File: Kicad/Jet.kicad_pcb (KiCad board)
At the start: 2 copper layers, 17 parts, among them J1 Conn_02x13_Odd_Even, J2 Conn_01x03_Female, J3 POWER, J4 Conn_02x10_Odd_Even, J5 Conn_02x10_Odd_Even, Q1 Q_NPN_EBC, Q2 Q_NPN_EBC, U1 PC817, U2 PC817

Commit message: UPDATE: footprint
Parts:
- D1, D3: value D_Zener -> BZM55C30-LGE; footprint Diode_THT:D_DO-35_SOD27_P7.62mm_Horizontal -> Diode_SMD:D_MiniMELF
- D2, D4: value 1N4448 -> M7L-DIO; footprint Diode_THT:D_DO-35_SOD27_P7.62mm_Horizontal -> Diode_SMD:D_SMA
- Q1, Q2: value Q_NPN_EBC -> BCW66FR; footprint Package_TO_SOT_THT:TO-92L_HandSolder -> Package_TO_SOT_SMD:SOT-23
- moved R3 85.3 mm to (112.6, 149.2), turned to 180 degrees
- moved D4 82.6 mm to (154.0, 29.6), turned to -90 degrees
- moved D3 80.8 mm to (156.9, 29.6)
- moved Q2 69.1 mm to (156.7, 40.8), turned to 180 degrees
- moved R4 68.0 mm to (156.3, 57.3), turned to 0 degrees
- moved R2 62.6 mm to (156.3, 45.0)
- moved U1 61.5 mm to (96.8, 139.5), turned to 180 degrees
- moved U2 57.1 mm to (154.1, 54.9)
- moved D1 55.0 mm to (112.6, 25.6), turned to 90 degrees
- moved D2 50.0 mm to (109.1, 25.8), turned to 90 degrees
- moved J1 23.2 mm to (96.6, 105.1)
- moved Q1 15.5 mm to (90.8, 60.9)
- moved R1 15.5 mm to (92.3, 55.4)
- moved J4 3.88 mm to (125.3, 78.0)
- moved J5 3.88 mm to (114.2, 78.0)
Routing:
- net GND: track 165.1 -> 0.00 mm, vias 1 -> 0
- net VCC: track 154.0 -> 0.00 mm
- net IN_AGREGAT_REKA: track 121.1 -> 0.00 mm
- net IN_AGREGAT_KRANCOWKA: track 107.8 -> 0.00 mm, vias 1 -> 0
- net IN_CONFIG2: track 107.0 -> 0.00 mm, vias 1 -> 0
- net IN_AGREGAT_RESET: track 100.6 -> 0.00 mm
- net IN_KOLO_KRANCOWKA: track 98.8 -> 0.00 mm, vias 1 -> 0
- net IN_INTERWAL: track 96.5 -> 0.00 mm, vias 1 -> 0
- net TIME+: track 91.3 -> 0.00 mm
- net IN_WANNA: track 91.0 -> 0.00 mm, vias 1 -> 0
- net IN_CONFIG1: track 86.9 -> 0.00 mm, vias 1 -> 0
- net IN_START: track 84.5 -> 0.00 mm, vias 1 -> 0
- net IN_OBUDOWA: track 64.7 -> 0.00 mm
- net TIME-: track 62.3 -> 0.00 mm
- net AGREGAT: track 26.6 -> 0.00 mm
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
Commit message: FIX PCB
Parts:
- moved D2 86.4 mm to (108.0, 112.2), turned to -90 degrees
- moved D1 83.8 mm to (105.0, 109.1), turned to -90 degrees
- moved D3 75.8 mm to (103.9, 83.7), turned to 90 degrees
- moved D4 74.3 mm to (107.0, 87.2)
- moved Q2 64.3 mm to (107.0, 81.5), turned to 90 degrees
- moved R2 62.6 mm to (103.8, 79.0), turned to -90 degrees
- moved R4 53.8 mm to (106.8, 78.4), turned to 180 degrees
- moved R1 50.6 mm to (104.9, 104.4), turned to 90 degrees
- moved Q1 48.9 mm to (108.1, 106.6)
- moved U2 48.9 mm to (107.1, 68.3), turned to -90 degrees
- moved U1 47.2 mm to (108.1, 93.6), turned to -90 degrees
- moved R3 45.9 mm to (107.9, 103.5)
- moved J2 29.0 mm to (102.3, 64.9), turned to 90 degrees
- moved J3 21.8 mm to (101.5, 114.7), turned to 90 degrees
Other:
- board text removed: "dół"
- board text removed: "góra"

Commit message: FIX PCB
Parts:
- moved J3 45.6 mm to (101.5, 69.1), turned to 0 degrees
- moved R2 3.40 mm to (101.1, 77.0)
- moved D1 3.07 mm to (102.0, 109.5)
- moved R1 3.05 mm to (101.9, 104.2)
- moved D3 2.56 mm to (101.4, 84.2)
- moved D4 1.32 mm to (107.3, 88.5)
- moved Q2 0.88 mm to (107.4, 82.3)
- moved Q1 0.71 mm to (107.4, 106.4)
- moved D2 0.69 mm to (107.4, 112.2)
- moved R3 0.67 mm to (107.3, 103.4)
- moved U1 0.58 mm to (107.6, 93.5)
- moved R4 0.57 mm to (107.3, 78.7)
- moved U2 0.44 mm to (107.6, 68.3)
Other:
- board outline added: 40.1 x 54.1 mm
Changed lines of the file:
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@@
   (net 53 "Net-(R2-Pad1)")
   (footprint "Resistor_SMD:R_0805_2012Metric_Pad1.20x1.40mm_HandSolder" (layer "F.Cu")
-    (at 106.84 78.36 180)
+    (at 107.265 78.74 180)
     (descr "Resistor SMD 0805 (2012 Metric), square (rectangular) end terminal, IPC_7351 nominal with elongated pad for handsoldering. (Body size source: IPC-SM-782 page 72, https://www.pcb-3d.com/wordpress/wp-content/uploads/ipc-sm-782a_amendment_1_and_2.pdf), generated with kicad-footprint-generator")
     (tags "resistor handsolder")
@@
   )
   (footprint "Diode_SMD:D_SMA" (layer "F.Cu")
-    (at 108.05 112.2 -90)
+    (at 107.365 112.2 -90)
     (descr "Diode SMA (DO-214AC)")
     (tags "Diode SMA (DO-214AC)")
@@
   )
   (footprint "Diode_SMD:D_MiniMELF" (layer "F.Cu")
-    (at 103.92 83.74 90)
+    (at 101.41 84.22 90)
     (descr "Diode Mini-MELF (SOD-80)")
     (tags "Diode Mini-MELF (SOD-80)")
@@
     (pad "20" thru_hole circle (at 2.54 22.86) (size 1.7 1.7) (drill 1) (layers *.Cu *.Mask)
       (net 2 "GND") (pinfunction "Pin_20") (pintype "passive"))
-    (pad "MP" thru_hole circle (at 1.02 -8.94) (size 8 8) (drill 2.69) (layers *.Cu *.Mask))
-    (pad "MP" thru_hole circle (at 1.02 31.8) (size 8 8) (drill 2.69) (layers *.Cu *.Mask))
+    (pad "MP" thru_hole circle (at 1.02 -8.94) (size 3.5 3.5) (drill 2.5) (layers *.Cu *.Mask))
+    (pad "MP" thru_hole circle (at 1.02 31.8) (size 3.5 3.5) (drill 2.5) (layers *.Cu *.Mask))
     (model "${KICAD6_3DMODEL_DIR}/Connector_IDC.3dshapes/IDC-Header_2x10-1MP_P2.54mm_Latch_Vertical.wrl"
       (offset (xyz 0 0 0))
@@
   )
   (footprint "Resistor_SMD:R_0805_2012Metric_Pad1.20x1.40mm_HandSolder" (layer "F.Cu")
-    (at 104.9 104.37 90)
+    (at 101.854 104.25 90)
     (descr "Resistor SMD 0805 (2012 Metric), square (rectangular) end terminal, IPC_7351 nominal with elongated pad for handsoldering. (Body size source: IPC-SM-782 page 72, https://www.pcb-3d.com/wordpress/wp-content/uploads/ipc-sm-782a_amendment_1_and_2.pdf), generated with kicad-footprint-generator")
     (tags "resistor handsolder")
@@
   )
   (footprint "Package_DIP:DIP-4_W7.62mm" (layer "F.Cu")
-    (at 108.125 93.63 -90)
+    (at 107.565 93.482 -90)
     (descr "4-lead though-hole mounted DIP package, row spacing 7.62 mm (300 mils)")
     (tags "THT DIP DIL PDIP 2.54mm 7.62mm 300mil")
@@
   )
   (footprint "Resistor_SMD:R_0805_2012Metric_Pad1.20x1.40mm_HandSolder" (layer "F.Cu")
-    (at 107.93 103.49 180)
+    (at 107.265 103.378 180)
     (descr "Resistor SMD 0805 (2012 Metric), square (rectangular) end terminal, IPC_7351 nominal with elongated pad for handsoldering. (Body size source: IPC-SM-782 page 72, https://www.pcb-3d.com/wordpress/wp-content/uploads/ipc-sm-782a_amendment_1_and_2.pdf), generated with kicad-footprint-generator")
     (tags "resistor handsolder")
@@
   )
   (footprint "Package_DIP:DIP-4_W7.62mm" (layer "F.Cu")
-    (at 107.12 68.34 -90)
+    (at 107.565 68.34 -90)
     (descr "4-lead though-hole mounted DIP package, row spacing 7.62 mm (300 mils)")
     (tags "THT DIP DIL PDIP 2.54mm 7.62mm 300mil")
@@
     (pad "26" thru_hole circle (at 2.54 30.48 180) (size 1.7 1.7) (drill 1) (layers *.Cu *.Mask)
       (net 30 "IN_OBUDOWA") (pinfunction "Pin_26") (pintype "passive"))
-    (pad "MP" thru_hole circle (at 1.8 -5.905 180) (size 8 8) (drill 2.69) (layers *.Cu *.Mask))
-    (pad "MP" thru_hole circle (at 1.8 36.385 180) (size 8 8) (drill 2.69) (layers *.Cu *.Mask))
+    (pad "MP" thru_hole circle (at 1.8 -5.905 180) (size 3.5 3.5) (drill 2.5) (layers *.Cu *.Mask))
+    (pad "MP" thru_hole circle (at 1.8 36.385 180) (size 3.5 3.5) (drill 2.5) (layers *.Cu *.Mask))
     (model "${KICAD6_3DMODEL_DIR}/Connector_IDC.3dshapes/IDC-Header_2x13-1MP_P2.54mm_Latch_Horizontal.wrl"
       (offset (xyz 0 0 0))
@@
   )
   (footprint "Package_TO_SOT_SMD:SOT-23" (layer "F.Cu")
-    (at 108.11 106.56 90)
+    (at 107.415 106.426 90)
     (descr "SOT, 3 Pin (https://www.jedec.org/system/files/docs/to-236h.pdf variant AB), generated with kicad-footprint-generator ipc_gullwing_generator.py")
     (tags "SOT TO_SOT_SMD")
@@
   )
   (footprint "Package_TO_SOT_SMD:SOT-23" (layer "F.Cu")
-    (at 106.99 81.53 90)
+    (at 107.415 82.296 90)
     (descr "SOT, 3 Pin (https://www.jedec.org/system/files/docs/to-236h.pdf variant AB), generated with kicad-footprint-generator ipc_gullwing_generator.py")
     (tags "SOT TO_SOT_SMD")
@@
     (pad "20" thru_hole circle (at 2.54 22.86) (size 1.7 1.7) (drill 1) (layers *.Cu *.Mask)
       (net 2 "GND") (pinfunction "Pin_20") (pintype "passive"))
-    (pad "MP" thru_hole circle (at 1.02 -8.94) (size 8 8) (drill 2.69) (layers *.Cu *.Mask))
-    (pad "MP" thru_hole circle (at 1.02 31.8) (size 8 8) (drill 2.69) (layers *.Cu *.Mask))
+    (pad "MP" thru_hole circle (at 1.02 -8.94) (size 3.5 3.5) (drill 2.5) (layers *.Cu *.Mask))
+    (pad "MP" thru_hole circle (at 1.02 31.8) (size 3.5 3.5) (drill 2.5) (layers *.Cu *.Mask))
     (model "${KICAD6_3DMODEL_DIR}/Connector_IDC.3dshapes/IDC-Header_2x10-1MP_P2.54mm_Latch_Vertical.wrl"
       (offset (xyz 0 0 0))
@@
   )
   (footprint "Connector_PinSocket_2.54mm:PinSocket_1x02_P2.54mm_Vertical" (layer "F.Cu")
-    (at 101.51 114.725 90)
+    (at 101.475 69.08)
     (descr "Through hole straight socket strip, 1x02, 2.54mm pitch, single row (from Kicad 4.0.7), script generated")
     (tags "Through hole socket strip THT 1x02 2.54mm single row")
@@
     (property "Sheetname" "")
     (attr through_hole)
-    (fp_text reference "J3" (at 0 -2.77 90) (layer "F.SilkS")
-      (effects (font (size 1 1) (thickness 0.15)))
-    )
-    (fp_text value "POWER" (at 0 5.31 90) (layer "F.Fab")
-      (effects (font (size 1 1) (thickness 0.15)))
-    )
-    (fp_text user "${REFERENCE}" (at 0 1.27) (layer "F.Fab")
+    (fp_text reference "J3" (at 0 -2.77) (layer "F.SilkS")
+      (effects (font (size 1 1) (thickness 0.15)))
+    )
+    (fp_text value "POWER" (at 0 5.31) (layer "F.Fab")
+      (effects (font (size 1 1) (thickness 0.15)))
+    )
+    (fp_text user "${REFERENCE}" (at 0 1.27 90) (layer "F.Fab")
       (effects (font (size 1 1) (thickness 0.15)))
     )
@@
     (fp_line (start 1.27 3.81) (end -1.27 3.81) (layer "F.Fab") (width 0.1))
     (fp_line (start -1.27 3.81) (end -1.27 -1.27) (layer "F.Fab") (width 0.1))
-    (pad "1" thru_hole rect (at 0 0 90) (size 1.7 1.7) (drill 1) (layers *.Cu *.Mask)
+    (pad "1" thru_hole rect (at 0 0) (size 1.7 1.7) (drill 1) (layers *.Cu *.Mask)
       (net 7 "VCC") (pinfunction "Pin_1") (pintype "passive"))
-    (pad "2" thru_hole oval (at 0 2.54 90) (size 1.7 1.7) (drill 1) (layers *.Cu *.Mask)
+    (pad "2" thru_hole oval (at 0 2.54) (size 1.7 1.7) (drill 1) (layers *.Cu *.Mask)
       (net 2 "GND") (pinfunction "Pin_2") (pintype "passive"))
     (model "${KICAD6_3DMODEL_DIR}/Connector_PinSocket_2.54mm.3dshapes/PinSocket_1x02_P2.54mm_Vertical.wrl"
@@
   )
   (footprint "Diode_SMD:D_MiniMELF" (layer "F.Cu")
-    (at 105.04 109.12 -90)
+    (at 102.004 109.55 -90)
     (descr "Diode Mini-MELF (SOD-80)")
     (tags "Diode Mini-MELF (SOD-80)")
@@
   )
   (footprint "Diode_SMD:D_SMA" (layer "F.Cu")
-    (at 106.97 87.23 -90)
+    (at 107.35 88.49 -90)
     (descr "Diode SMA (DO-214AC)")
     (tags "Diode SMA (DO-214AC)")
@@
   )
   (footprint "Resistor_SMD:R_0805_2012Metric_Pad1.20x1.40mm_HandSolder" (layer "F.Cu")
-    (at 103.76 79.02 -90)
+    (at 101.06 76.95 -90)
     (descr "Resistor SMD 0805 (2012 Metric), square (rectangular) end terminal, IPC_7351 nominal with elongated pad for handsoldering. (Body size source: IPC-SM-782 page 72, https://www.pcb-3d.com/wordpress/wp-content/uploads/ipc-sm-782a_amendment_1_and_2.pdf), generated with kicad-footprint-generator")
     (tags "resistor handsolder")
@@
     )
   )
+  (gr_rect (start 91.694 62.738) (end 131.826 116.84) (layer "Edge.Cuts") (width 0.1) (fill none))
 )

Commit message: FIX PCB
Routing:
- net GND: track 0.00 -> 119.4 mm
- net VCC: track 0.00 -> 76.4 mm
- net IN_AGREGAT_RESET: track 0.00 -> 65.9 mm
- net IN_AGREGAT_REKA: track 0.00 -> 52.4 mm
- net KOLO: track 0.00 -> 46.2 mm, vias 0 -> 1
- net TIME+: track 0.00 -> 40.6 mm
- net IN_OBUDOWA: track 0.00 -> 38.9 mm
- net TIME-: track 0.00 -> 37.5 mm, vias 0 -> 2
- net IN_WANNA: track 0.00 -> 32.7 mm
- net IN_START: track 0.00 -> 32.6 mm
- net IN_AGREGAT_KRANCOWKA: track 0.00 -> 32.6 mm
- net IN_CONFIG2: track 0.00 -> 32.6 mm
- net IN_KOLO_KRANCOWKA: track 0.00 -> 32.6 mm
- net IN_INTERWAL: track 0.00 -> 32.6 mm
- net IN_CONFIG1: track 0.00 -> 32.6 mm
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
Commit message: FIX: PCB
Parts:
- moved D2 0.73 mm to (106.8, 112.6)
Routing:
- net Net-(Q2-Pad2): track 9.49 -> 13.0 mm, vias 0 -> 2
- net VCC: track 76.4 -> 78.8 mm
- net IN_AGREGAT_RESET: track 65.9 -> 68.2 mm
- net Net-(Q1-Pad2): track 7.39 -> 9.63 mm, vias 0 -> 2
- net GND: track 119.4 -> 120.3 mm, vias 0 -> 5
- net OK1: track 20.4 -> 21.3 mm
- net IN_OBUDOWA: track 38.9 -> 39.7 mm
- added copper zone on B.Cu, net GND
- added copper zone on F.Cu, net GND

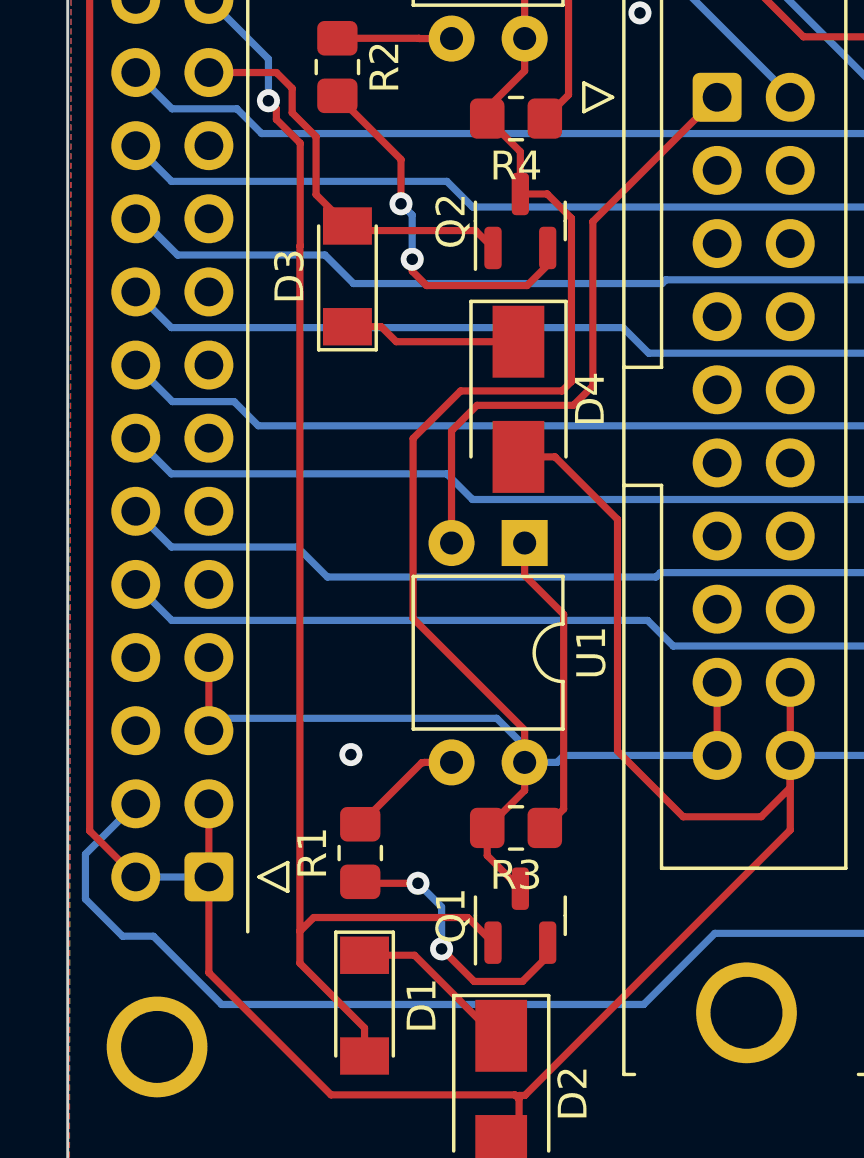
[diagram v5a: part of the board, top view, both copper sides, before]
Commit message: FIX Transistor footprin
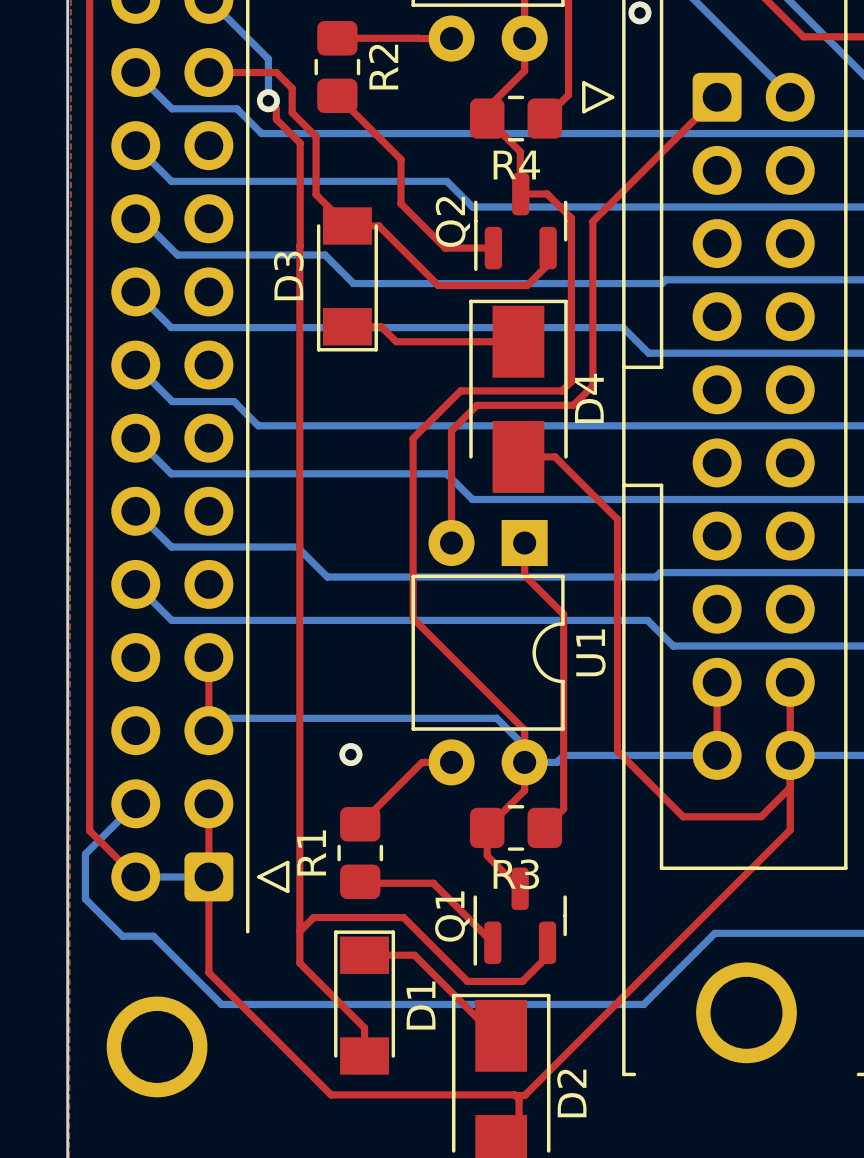
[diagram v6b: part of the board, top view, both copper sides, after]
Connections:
- Q1 pad 1: KOLO -> Net-(Q1-Pad1)
- Q1 pad 2: Net-(Q1-Pad2) -> KOLO
- Q2 pad 1: AGREGAT -> Net-(Q2-Pad1)
- Q2 pad 2: Net-(Q2-Pad2) -> AGREGAT
- R1 pad 1: Net-(Q1-Pad2) -> Net-(Q1-Pad1)
- R2 pad 2: Net-(Q2-Pad2) -> Net-(Q2-Pad1)
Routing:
- net Net-(Q2-Pad2): track 13.0 -> 0.00 mm, vias 2 -> 0
- net Net-(Q1-Pad2): track 9.63 -> 0.00 mm, vias 2 -> 0
- net Net-(Q2-Pad1): track 0.00 -> 8.51 mm
- net Net-(Q1-Pad1): track 0.00 -> 5.48 mm
- net AGREGAT: track 14.1 -> 17.4 mm
- net KOLO: track 46.2 -> 49.5 mm

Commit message: FIX: Paths
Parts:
- moved D1 0.55 mm to (102.0, 110.1)
- moved D2 0.55 mm to (106.8, 113.2)
- moved R1 0.55 mm to (101.9, 104.8)
- moved R3 0.55 mm to (107.3, 103.9)
- moved U1 0.55 mm to (107.6, 94.0)
- moved Q1 0.55 mm to (107.4, 107.0)
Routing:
- net GND: track 120.3 -> 0.00 mm, vias 5 -> 11
- net VCC: track 78.8 -> 80.5 mm
- net AGREGAT: track 17.4 -> 19.0 mm
- net IN_WANNA: track 32.7 -> 33.4 mm
